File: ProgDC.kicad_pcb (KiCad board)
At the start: 2 copper layers, 145 x 100 mm, 45 parts, among them J1 Conn_02x20_Counter_Clockwise_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, J2 Conn_01x24_Pin, J3 Conn_01x03_Pin, U1 KR580VK28, U2 628512, U3 CPU

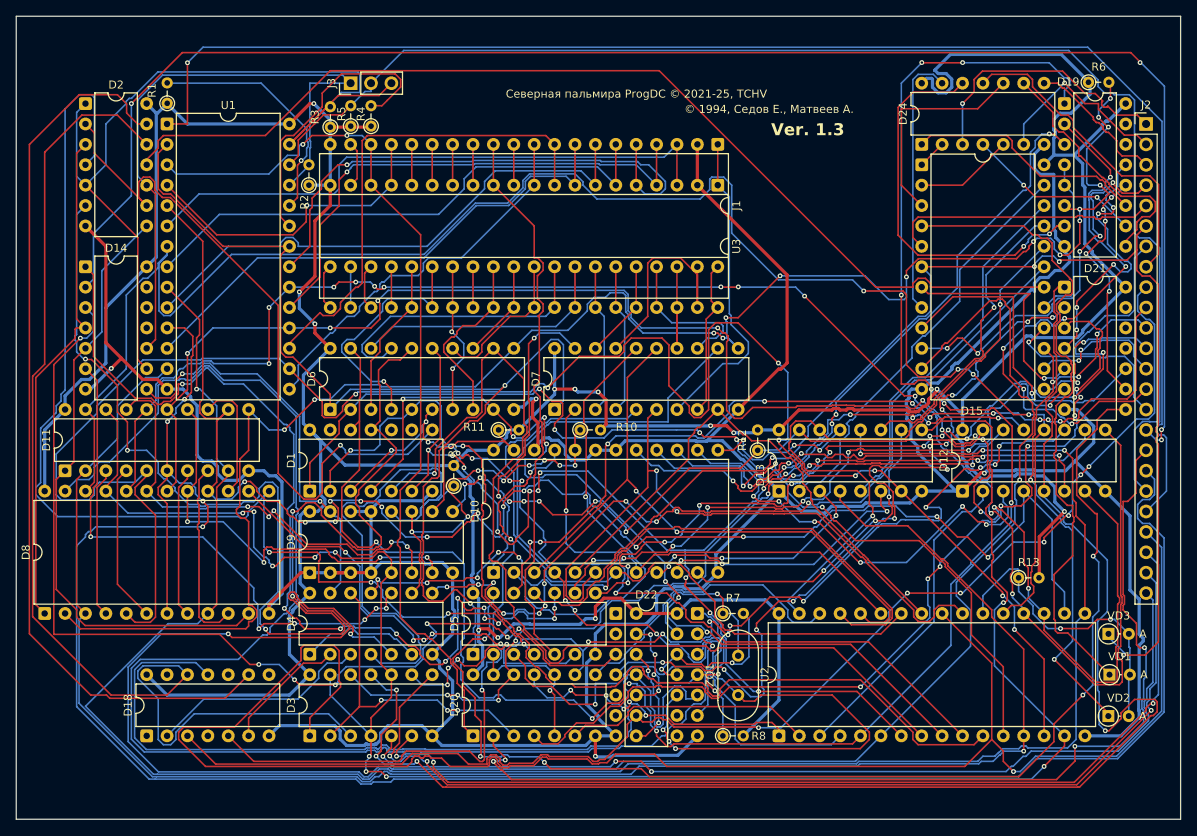
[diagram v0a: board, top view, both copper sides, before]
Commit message: Fix address and data buffering
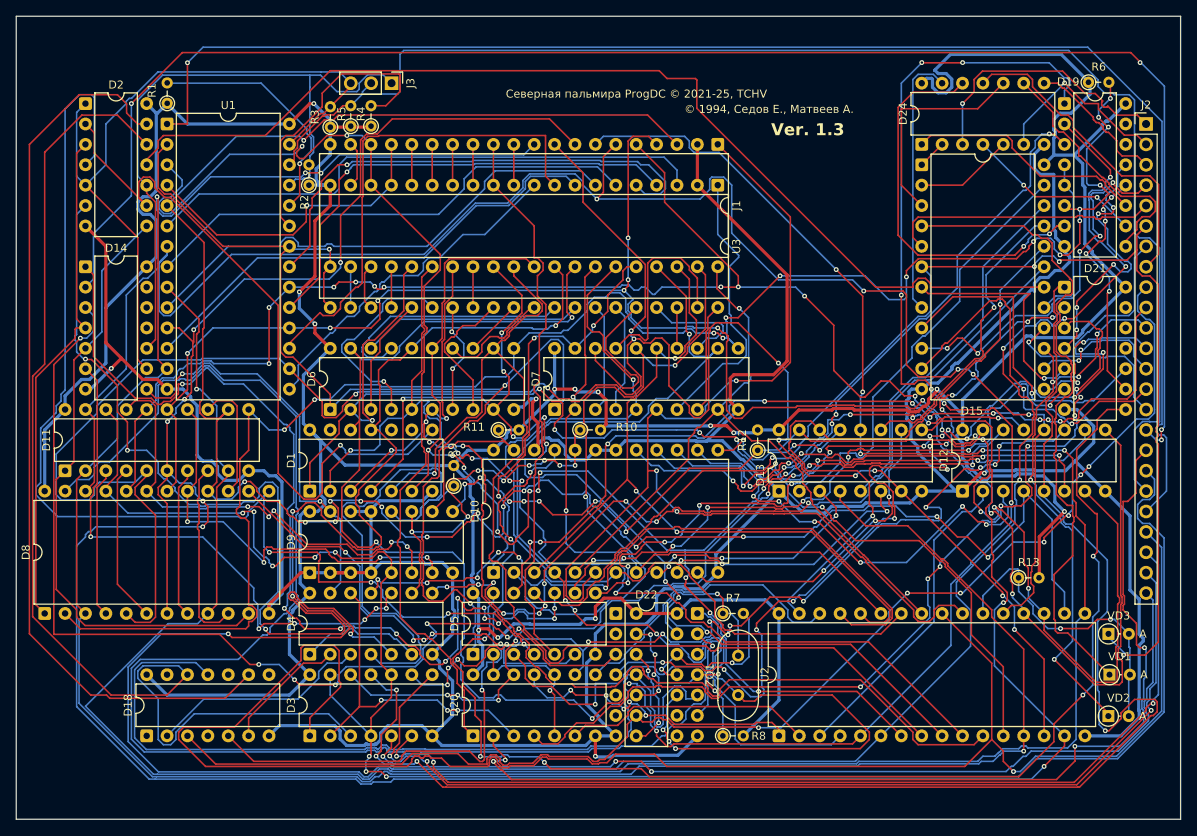
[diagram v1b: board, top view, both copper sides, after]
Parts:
- moved J3 5.10 mm to (88.9, 40.6), turned to -90 degrees
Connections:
- J1 pad 1: /A10 -> /AB10
- J1 pad 10: /D0 -> /DB0
- J1 pad 21: /_HLDA -> /HLDA
- J1 pad 25: /A0 -> /AB0
- J1 pad 26: /A1 -> /AB1
- J1 pad 27: /A2 -> /AB2
- J1 pad 29: /A3 -> /AB3
- J1 pad 3: /D4 -> /DB4
- J1 pad 30: /A4 -> /AB4
- J1 pad 31: /A5 -> /AB5
- J1 pad 32: /A6 -> /AB6
- J1 pad 33: /A7 -> /AB7
- J1 pad 34: /A8 -> /AB8
- J1 pad 35: /A9 -> /AB9
- J1 pad 36: /A15 -> /AB15
- J1 pad 37: /A12 -> /AB12
- J1 pad 38: /A13 -> /AB13
- J1 pad 39: /A14 -> /AB14
- J1 pad 4: /D5 -> /DB5
- J1 pad 40: /A11 -> /AB11
- J1 pad 5: /D6 -> /DB6
- J1 pad 6: /D7 -> /DB7
- J1 pad 7: /D3 -> /DB3
- J1 pad 8: /D2 -> /DB2
- J1 pad 9: /D1 -> /DB1
- U3 pad 21: /_HLDA -> /HLDA
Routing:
- net /DB0: track 216.7 -> 291.4 mm, vias 1 -> 4
- net /DB4: track 196.4 -> 266.6 mm, vias 14 -> 15
- net /DB2: track 272.2 -> 341.3 mm, vias 6 -> 8
- net /DB3: track 261.3 -> 320.4 mm, vias 4 -> 6
- net /AB10: track 85.2 -> 136.6 mm, vias 2 -> 3
- net /AB7: track 246.2 -> 283.9 mm, vias 10 -> 11
- net /DB1: track 236.0 -> 273.4 mm, vias 8 -> 10
- net /DB6: track 209.2 -> 238.4 mm
- net /AB6: track 308.2 -> 335.5 mm, vias 8 -> 9
- net /AB0: track 126.7 -> 152.8 mm, vias 5 -> 6
- net /AB14: track 56.0 -> 81.0 mm, vias 1 -> 2
- net /DB5: track 213.0 -> 236.7 mm, vias 11 -> 14
- net /AB5: track 190.7 -> 213.7 mm
- net /AB9: track 89.1 -> 111.5 mm, vias 0 -> 1
- net /AB2: track 109.3 -> 131.1 mm, vias 8 -> 9
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
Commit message: Ver. 1.4
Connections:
- D14 pad 11: unconnected-(D14.4-Y-Pad11) -> Net-(D14.4-Y)
- D14 pad 12: unconnected-(D14.4-A-Pad12) -> Net-(D14.4-A)
- D14 pad 13: unconnected-(D14.4-B-Pad13) -> Net-(D14.4-B)
- D19 pad 1: /AB7 -> /AB5
- D19 pad 3: /AB5 -> /AB7
- D21 pad 11: unconnected-(D21.4-Y-Pad11) -> /~{CS_DMA_2}
- D21 pad 12: unconnected-(D21.4-A-Pad12) -> Net-(D21.4-A)
- D21 pad 13: unconnected-(D21.4-B-Pad13) -> Net-(D14.4-Y)
- D22 pad 1: unconnected-(D22.1-A-Pad1) -> /~{WR}
- D22 pad 2: unconnected-(D22.1-Y-Pad2) -> Net-(D14.4-A)
- D22 pad 5: unconnected-(D22.3-A-Pad5) -> /~{CS_RAMR}
- D22 pad 6: unconnected-(D22.3-Y-Pad6) -> Net-(D14.4-B)
- D22 pad 8: unconnected-(D22.4-Y-Pad8) -> Net-(D21.4-A)
- D22 pad 9: unconnected-(D22.4-A-Pad9) -> /~{CS_DMA_}
- J2 pad 8: /~{CS_DMA_} -> /~{CS_DMA_2}
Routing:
- net Net-(D14.4-Y): track 0.00 -> 189.8 mm, vias 0 -> 5
- net Net-(D14.4-A): track 0.00 -> 135.9 mm, vias 0 -> 5
- net Net-(D14.4-B): track 0.00 -> 122.8 mm, vias 0 -> 5
- net Net-(D21.4-A): track 0.00 -> 120.7 mm, vias 0 -> 4
- net /~{CS_RAMR}: track 82.3 -> 170.5 mm, vias 0 -> 1
- net /~{CS_DMA_}: track 40.0 -> 107.5 mm, vias 0 -> 8
- net /~{WR}: track 127.3 -> 152.2 mm, vias 2 -> 6
- net /~{CS_DMA_2}: track 0.00 -> 12.5 mm
- net /AB7: track 283.9 -> 291.7 mm, vias 11 -> 12
- net +5V: track 525.0 -> 518.8 mm
- net /AB15: track 52.7 -> 58.4 mm
- net /AB4: track 140.2 -> 145.4 mm
- net /AB5: track 213.7 -> 218.1 mm, vias 15 -> 14
- net /8MHZ: track 110.0 -> 114.1 mm
- net /~{MEMW_VT57}: track 128.6 -> 132.6 mm
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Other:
- board text added: "Ver. 1.4"
- board text removed: "Ver. 1.3"

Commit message: Fix
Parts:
- added C1: 470, Capacitor_THT:C_Disc_D3.0mm_W1.6mm_P2.50mm, F.Cu at (181.4, 111.4)
- added D16: 133LL1, Package_DIP:DIP-14_W7.62mm, F.Cu at (137.0, 102.7)
- added R14: R0125, Resistor_THT:R_Axial_DIN0204_L3.6mm_D1.6mm_P2.54mm_Vertical, F.Cu at (157.9, 97.6)
- added VD4: 1N4148, Diode_THT:D_DO-34_SOD68_P2.54mm_Vertical_AnodeUp, F.Cu at (157.9, 101.4)
- added VD5: 1N4148, Diode_THT:D_DO-34_SOD68_P2.54mm_Vertical_AnodeUp, F.Cu at (157.8, 95.2)
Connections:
- D14 pad 11: Net-(D14.4-Y) -> unconnected-(D14.4-Y-Pad11)
- D14 pad 12: Net-(D14.4-A) -> unconnected-(D14.4-A-Pad12)
- D14 pad 13: Net-(D14.4-B) -> unconnected-(D14.4-B-Pad13)
- D21 pad 12: Net-(D21.4-A) -> GND
- D21 pad 13: Net-(D14.4-Y) -> Net-(D21.4-B)
- D22 pad 1: /~{WR} -> unconnected-(D22.1-A-Pad1)
- D22 pad 2: Net-(D14.4-A) -> unconnected-(D22.1-Y-Pad2)
- D22 pad 6: Net-(D14.4-B) -> /CS_RAMR
- D22 pad 8: Net-(D21.4-A) -> unconnected-(D22.4-Y-Pad8)
- D22 pad 9: /~{CS_DMA_} -> unconnected-(D22.4-A-Pad9)
- D4 pad 13: Net-(D14.3-Y) -> Net-(D16.4-Y)
- U2 pad 29: /~{WE_628512} -> Net-(D16.1-Y)
- U2 pad 31: /R3 -> /AB15
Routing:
- net Net-(D14.4-Y): track 189.8 -> 0.00 mm, vias 5 -> 0
- net Net-(D14.4-A): track 135.9 -> 0.00 mm, vias 5 -> 0
- net Net-(D14.4-B): track 122.8 -> 0.00 mm, vias 5 -> 0
- net Net-(D21.4-A): track 120.7 -> 0.00 mm, vias 4 -> 0
- net /~{WR}: track 152.2 -> 265.5 mm, vias 6 -> 7
- net Net-(D16.4-Y): track 0.00 -> 73.7 mm, vias 0 -> 4
- net Net-(D14.3-Y): track 51.3 -> 106.0 mm, vias 2 -> 9
- net /CS_RAMR: track 0.00 -> 53.6 mm
- net Net-(D21.4-B): track 0.00 -> 50.0 mm, vias 0 -> 1
- net /AB15: track 58.4 -> 104.7 mm, vias 3 -> 8
- net /R3: track 83.6 -> 42.8 mm, vias 2 -> 1
- net GND: track 510.5 -> 546.9 mm, vias 4 -> 6
- net /~{CS_628512}: track 38.7 -> 75.1 mm, vias 2 -> 3
- net /~{WE_628512}: track 89.9 -> 59.3 mm
- net /~{CS_RAMR}: track 170.5 -> 197.9 mm, vias 1 -> 6
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
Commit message: Fix layout
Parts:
- moved J2 0.40 mm to (183.3, 45.7)
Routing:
- net /DB4: track 290.5 -> 282.4 mm
- net Net-(D19-3): track 35.7 -> 31.4 mm
- net GND: track 546.9 -> 542.8 mm
- net /AB7: track 301.5 -> 297.9 mm
- net Net-(D14.1-A): track 122.0 -> 119.0 mm
- net /AB10: track 142.5 -> 139.7 mm
- net /"1": track 216.7 -> 214.0 mm
- net /C800_VI53_2: track 150.0 -> 147.5 mm
- net /CLK: track 170.6 -> 168.2 mm
- net /~{RD}: track 216.9 -> 214.7 mm
- net Net-(D21.2-A): track 35.3 -> 33.2 mm
- net Net-(D22.5-Y): track 65.7 -> 63.9 mm
- net /8MHZ: track 111.7 -> 109.9 mm
- net Net-(D20.2-A): track 116.7 -> 114.9 mm
- net Net-(D21.1-B): track 105.9 -> 104.3 mm
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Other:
- board text added: "ProgDC Северная пальмира"
- board text added: "© 2021-25, TCHV"
- board text removed: "Северная пальмира ProgDC © 2021-25, TCHV"

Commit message: Update PCB
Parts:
- added D17: КР1533КП11, Package_DIP:DIP-16_W7.62mm, F.Cu at (44.7, 111.4)
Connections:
- D10 pad 12: GND -> unconnected-(D10-GND-Pad12)
- D10 pad 19: GND -> Net-(D10-A0)
- D10 pad 22: GND -> Net-(D10-A1)
- D10 pad 24: +5V -> unconnected-(D10-VCC-Pad24)
- D12 pad 10: Net-(D10-D6) -> Net-(D10-D2)
- D12 pad 11: /R6 -> /R2
- D12 pad 12: /DB7 -> /DB3
- D12 pad 13: Net-(D10-D7) -> Net-(D10-D3)
- D12 pad 14: /R7 -> /R3
- D12 pad 2: /R4 -> /R0
- D12 pad 3: Net-(D10-D4) -> Net-(D10-D0)
- D12 pad 4: /DB4 -> /DB0
- D12 pad 5: /R5 -> /R1
- D12 pad 6: Net-(D10-D5) -> Net-(D10-D1)
- D12 pad 7: /DB5 -> /DB1
- D12 pad 9: /DB6 -> /DB2
- D13 pad 10: Net-(D10-D2) -> Net-(D10-D6)
- D13 pad 11: /R2 -> /R6
- D13 pad 12: /DB3 -> /DB7
- D13 pad 13: Net-(D10-D3) -> Net-(D10-D7)
- D13 pad 14: /R3 -> /R7
- D13 pad 2: /R0 -> /R4
- D13 pad 3: Net-(D10-D0) -> Net-(D10-D4)
- D13 pad 4: /DB0 -> /DB4
- D13 pad 5: /R1 -> /R5
- D13 pad 6: Net-(D10-D1) -> Net-(D10-D5)
- D13 pad 7: /DB1 -> /DB5
- D13 pad 9: /DB2 -> /DB6
- D9 pad 15: Net-(D14.3-Y) -> GND
- D9 pad 4: GND -> Net-(D14.3-Y)
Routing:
- net Net-(D10-A1): track 0.00 -> 114.8 mm, vias 0 -> 3
- net Net-(D10-A0): track 0.00 -> 105.1 mm, vias 0 -> 7
- net GND: track 542.8 -> 632.9 mm, vias 6 -> 11
- net /P3: track 84.0 -> 161.6 mm, vias 7 -> 11
- net /Q4: track 17.6 -> 72.5 mm, vias 0 -> 2
- net /DB6: track 239.3 -> 190.8 mm, vias 12 -> 10
- net /R5: track 176.1 -> 132.5 mm, vias 3 -> 6
- net Net-(D10-D4): track 61.0 -> 20.1 mm, vias 6 -> 3
- net Net-(D10-D2): track 40.8 -> 76.0 mm, vias 3 -> 6
- net /Q3: track 23.2 -> 56.2 mm, vias 0 -> 2
- net /R6: track 112.6 -> 81.9 mm, vias 14 -> 6
- net Net-(D10-D3): track 20.1 -> 49.4 mm, vias 3 -> 4
- net /Q1: track 19.7 -> 48.9 mm, vias 0 -> 1
- net Net-(D10-D7): track 57.8 -> 29.0 mm, vias 6 -> 2
- net /DB1: track 277.4 -> 306.2 mm, vias 10 -> 12
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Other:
- board text added: "BLUE"
- board text added: "RED"
- board text added: "YELLOW"

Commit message: Fix pcb
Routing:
- net /AB9: track 118.7 -> 133.3 mm
- net /A15: track 21.3 -> 7.18 mm
- net GND: track 632.9 -> 623.6 mm
- net /DB1: track 306.2 -> 299.1 mm
- net Net-(D21.1-B): track 115.8 -> 112.1 mm
- net /AB13: track 100.4 -> 97.4 mm
- net Net-(D5.2-A): track 206.7 -> 204.5 mm
- net /Q4: track 72.5 -> 70.5 mm
- net /A9: track 13.6 -> 15.6 mm
- net /AB6: track 347.8 -> 345.8 mm
- net /A8: track 13.6 -> 15.6 mm
- net /A14: track 25.9 -> 27.7 mm
- net /DB5: track 208.6 -> 206.8 mm
- net Net-(D10-D5): track 42.9 -> 41.3 mm
- net /DB3: track 327.3 -> 325.8 mm
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
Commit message: Fix bugs
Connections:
- net /~{CA00_PPI3} renamed /~{C500_VDP}
- D10 pad 12: unconnected-(D10-GND-Pad12) -> GND
- D10 pad 24: unconnected-(D10-VCC-Pad24) -> +5V
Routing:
- net /AB15: track 104.4 -> 98.4 mm
- net +5V: track 548.7 -> 550.8 mm
- net /AB9: track 133.3 -> 132.5 mm
- net /~{CC00_VI53_1_}: track 116.9 -> 116.2 mm
- net /AB13: track 97.4 -> 96.8 mm
- net GND: track 623.6 -> 623.0 mm

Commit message: Fix bugs
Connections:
- net Net-(D2.1-B) renamed /~{A_FF}
- D9 pad 15: GND -> Net-(D14.3-Y)
- D9 pad 4: Net-(D14.3-Y) -> GND
- R8 pad 1: Net-(D23.1-~{R}) -> unconnected-(R8-Pad1)
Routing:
- net Net-(D14.3-Y): track 123.6 -> 111.7 mm, vias 11 -> 10
- net GND: track 623.0 -> 615.3 mm, vias 11 -> 10
- net /P0: track 75.4 -> 70.5 mm
- net /AB6: track 345.8 -> 343.9 mm
- net /~{RESET}: track 60.7 -> 59.7 mm
- net /Q7: track 234.6 -> 233.7 mm
- net /Q6: track 56.0 -> 55.4 mm
